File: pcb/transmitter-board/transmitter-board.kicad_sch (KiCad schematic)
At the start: 26 parts, among them J1 USB-C_USB-310F-B-SU, Q3 AO3400A, Q4 AO3400A, SW1 SW_DPDT_x2, U1 NE555D, U3 TP4056-42-ESOP8, U4 DW01A

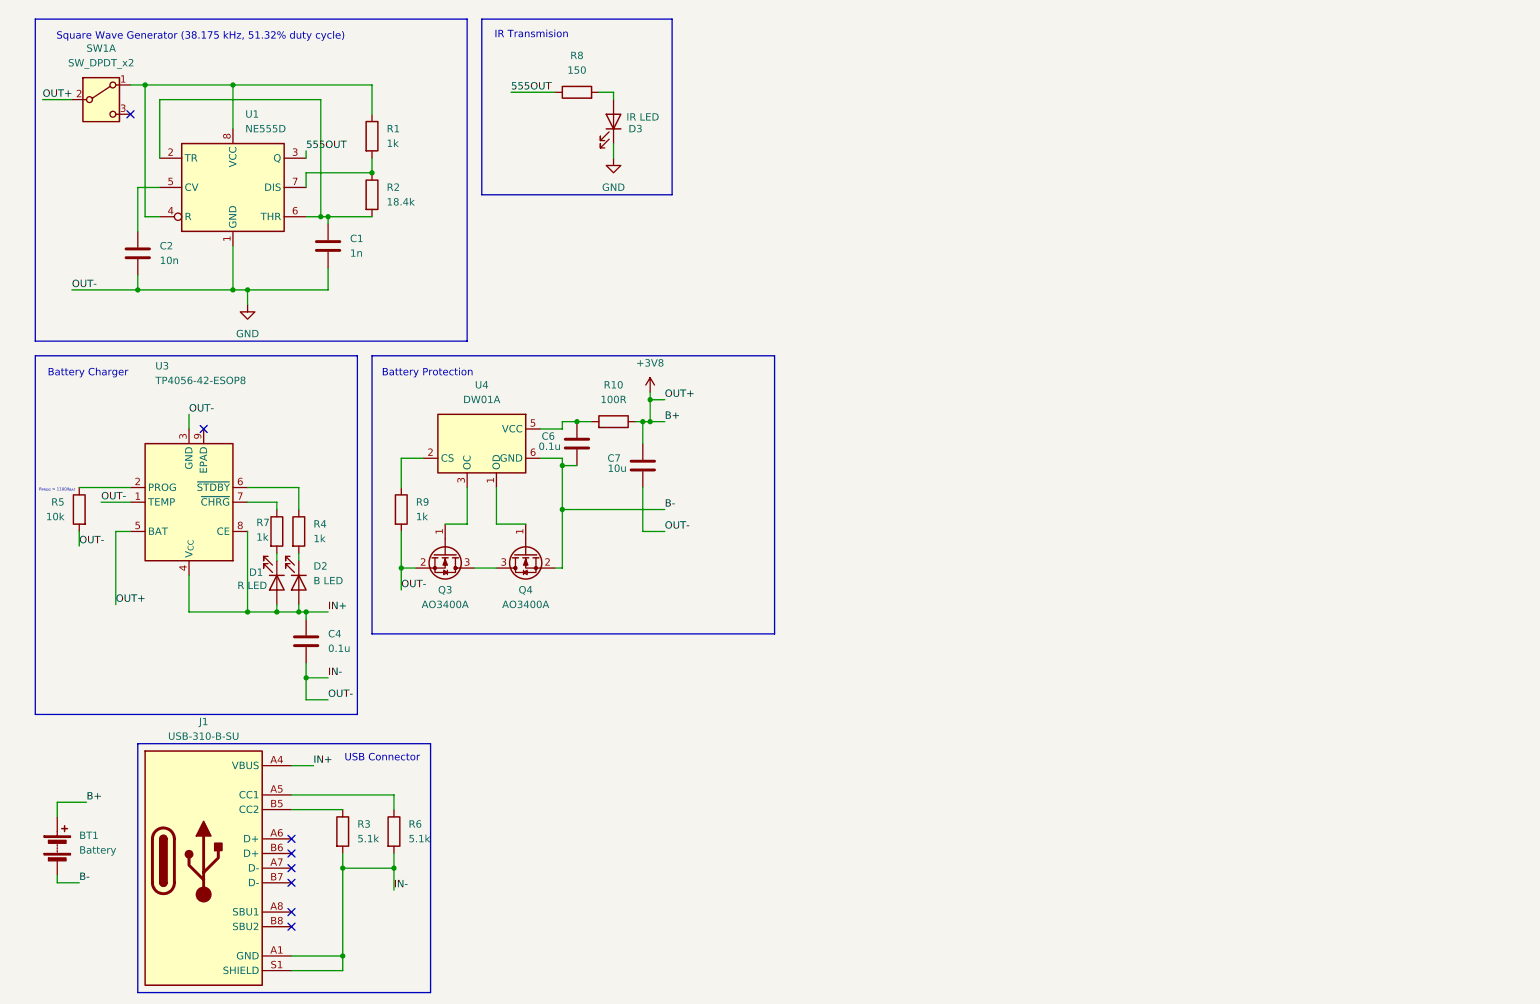
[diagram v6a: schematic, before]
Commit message: Edited transmitter-board schematic
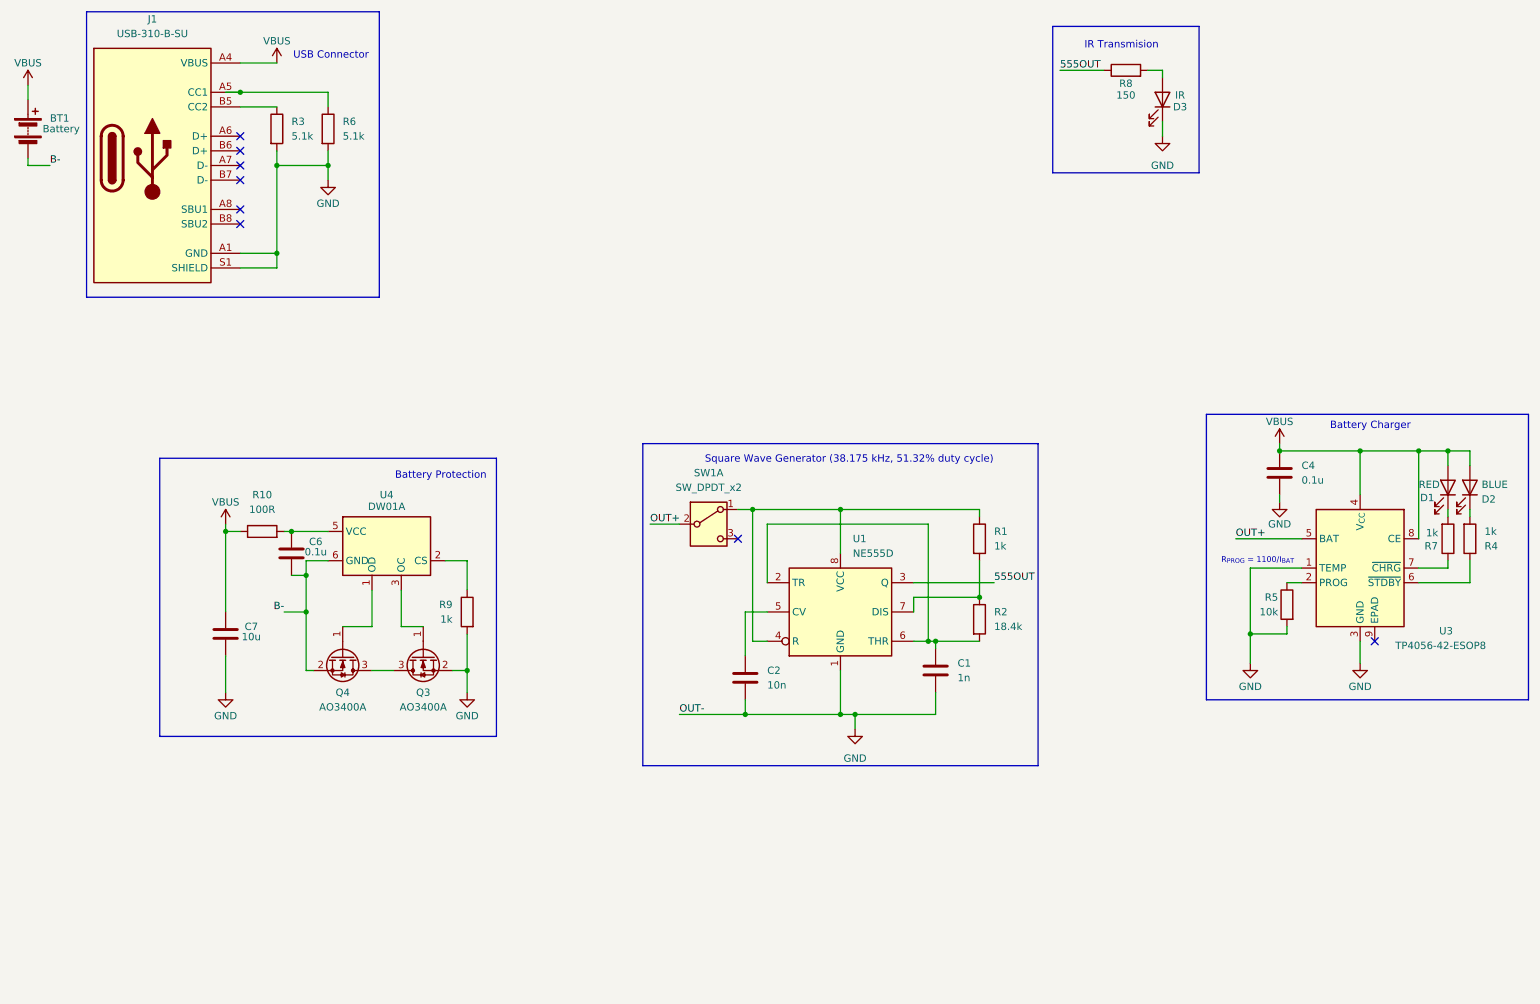
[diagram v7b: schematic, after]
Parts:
- D1: value R LED -> RED
- D2: value B LED -> BLUE
- D3: value IR LED -> IR
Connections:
- net IN+ is gone; now on net VBUS: C4.1, D1.2 (A), D2.2 (A), J1.A4 (VBUS), J1.A9 (VBUS), J1.B4 (VBUS), J1.B9 (VBUS), U3.4 (V_{CC}), U3.8 (CE)
- net +3V8 renamed VBUS
- net VBUS: no longer SW1.2 (B), U3.5 (BAT)
- new net OUT+: SW1.2 (B), U3.5 (BAT)
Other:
- moved on the sheet: BT1, C1, C2, C4, C6, C7, D1, D2, D3, J1, Q3, Q4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

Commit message: Change schematic look
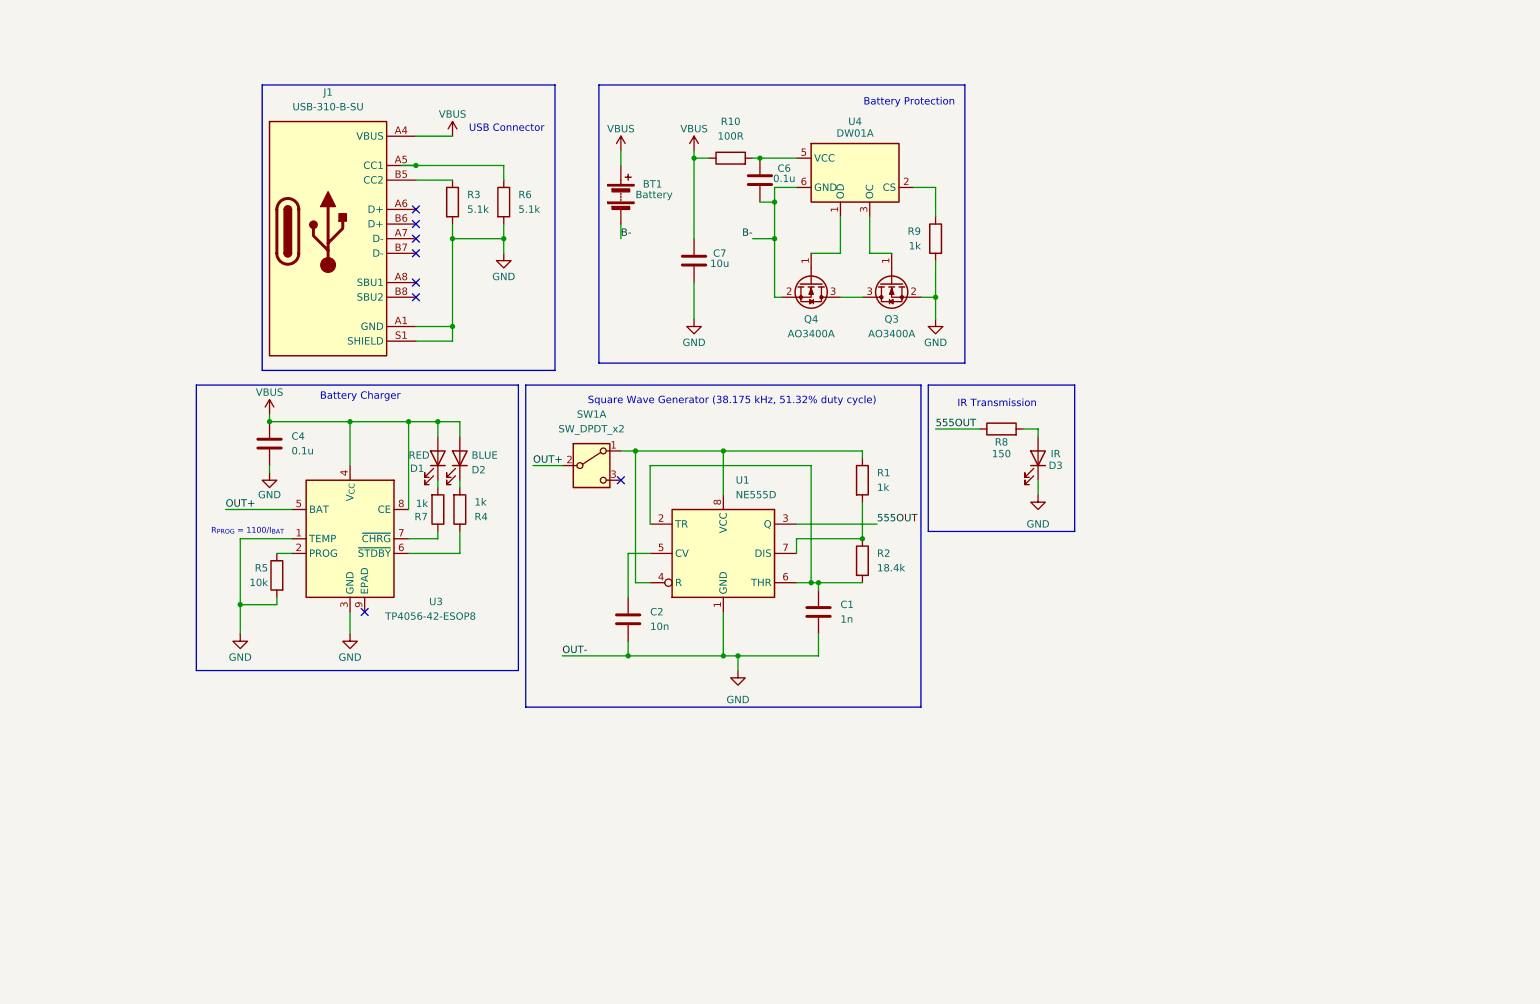
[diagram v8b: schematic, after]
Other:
- note added: "IR Transmission"
- note removed: "IR Transmision"
- moved on the sheet: BT1, C1, C2, C4, C6, C7, D1, D2, D3, J1, Q3, Q4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
